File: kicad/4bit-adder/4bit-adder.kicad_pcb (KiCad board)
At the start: 2 copper layers, 4 parts

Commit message: footprints initial layout
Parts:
- added C1: 100uF, Capacitor_THT:CP_Radial_D10.0mm_P2.50mm, F.Cu at (128.5, 214.1)
- added D1: 1N4001, Diode_THT:D_DO-41_SOD81_P10.16mm_Horizontal, F.Cu at (112.1, 51.3)
- added D10: A4 Yellow, LED_THT:LED_D3.0mm, F.Cu at (70.1, 31.3)
- added D11: Carry2 White, LED_THT:LED_D3.0mm, F.Cu at (95.8, 26.8)
- added D12: Carry3 White, LED_THT:LED_D3.0mm, F.Cu at (70.1, 26.8)
- added D13: Sum2 Red, LED_THT:LED_D3.0mm, F.Cu at (96.0, 217.8)
- added D14: Sum3 Red, LED_THT:LED_D3.0mm, F.Cu at (83.1, 217.8)
- added D15: B4 Green, LED_THT:LED_D3.0mm, F.Cu at (70.1, 35.7)
- added D16: A3 Yellow, LED_THT:LED_D3.0mm, F.Cu at (95.8, 31.3)
- added D17: B3 Green, LED_THT:LED_D3.0mm, F.Cu at (95.8, 35.8)
- added D18: A2 Yellow, LED_THT:LED_D3.0mm, F.Cu at (120.6, 31.3)
- added D19: B2 Green, LED_THT:LED_D3.0mm, F.Cu at (120.6, 35.8)
- added D2: A1 Yellow, LED_THT:LED_D3.0mm, F.Cu at (138.9, 31.5)
- added D20: Sum4 Red, LED_THT:LED_D3.0mm, F.Cu at (70.2, 217.7)
- added D21: B1 Green, LED_THT:LED_D3.0mm, F.Cu at (138.9, 36.0)
- added D22: 1N4001, Diode_THT:D_DO-41_SOD81_P10.16mm_Horizontal, F.Cu at (61.1, 52.0)
- added D23: 1N4001, Diode_THT:D_DO-41_SOD81_P10.16mm_Horizontal, F.Cu at (61.1, 67.9)
- added D24: 1N4001, Diode_THT:D_DO-41_SOD81_P10.16mm_Horizontal, F.Cu at (61.1, 73.7)
- added D25: Carry4 Red, LED_THT:LED_D3.0mm, F.Cu at (57.5, 217.5)
- added D26: 1N4001, Diode_THT:D_DO-41_SOD81_P10.16mm_Horizontal, F.Cu at (143.7, 62.4)
- added D27: 1N4001, Diode_THT:D_DO-41_SOD81_P10.16mm_Horizontal, F.Cu at (143.7, 86.7)
- added D28: 1N4001, Diode_THT:D_DO-41_SOD81_P10.16mm_Horizontal, F.Cu at (143.7, 111.2)
- added D29: 1N4001, Diode_THT:D_DO-41_SOD81_P10.16mm_Horizontal, F.Cu at (125.6, 62.4)
- added D3: 1N4001, Diode_THT:D_DO-41_SOD81_P10.16mm_Horizontal, F.Cu at (112.3, 67.5)
- added D30: 1N4001, Diode_THT:D_DO-41_SOD81_P10.16mm_Horizontal, F.Cu at (125.5, 86.5)
- added D31: 1N4001, Diode_THT:D_DO-41_SOD81_P10.16mm_Horizontal, F.Cu at (125.5, 110.8)
- added D32: 1N4001, Diode_THT:D_DO-41_SOD81_P10.16mm_Horizontal, F.Cu at (125.4, 134.8)
- added D33: 1N4001, Diode_THT:D_DO-41_SOD81_P10.16mm_Horizontal, F.Cu at (125.4, 159.1)
- added D34: 1N4001, Diode_THT:D_DO-41_SOD81_P10.16mm_Horizontal, F.Cu at (125.3, 207.6)
- added D35: 1N4001, Diode_THT:D_DO-41_SOD81_P10.16mm_Horizontal, F.Cu at (100.2, 207.4)
- added D36: 1N4001, Diode_THT:D_DO-41_SOD81_P10.16mm_Horizontal, F.Cu at (74.2, 208.3)
- added D37: 1N4001, Diode_THT:D_DO-41_SOD81_P10.16mm_Horizontal, F.Cu at (74.2, 184.0)
- added D38: 1N4001, Diode_THT:D_DO-41_SOD81_P10.16mm_Horizontal, F.Cu at (100.2, 183.2)
- added D39: 1N4001, Diode_THT:D_DO-41_SOD81_P10.16mm_Horizontal, F.Cu at (100.2, 159.1)
- added D4: 1N4001, Diode_THT:D_DO-41_SOD81_P10.16mm_Horizontal, F.Cu at (112.2, 73.3)
- added D40: 1N4001, Diode_THT:D_DO-41_SOD81_P10.16mm_Horizontal, F.Cu at (74.2, 159.8)
- added D41: 1N4001, Diode_THT:D_DO-41_SOD81_P10.16mm_Horizontal, F.Cu at (100.2, 134.9)
- added D42: 1N4001, Diode_THT:D_DO-41_SOD81_P10.16mm_Horizontal, F.Cu at (74.2, 135.5)
- added D43: 1N4001, Diode_THT:D_DO-41_SOD81_P10.16mm_Horizontal, F.Cu at (74.3, 111.3)
- added D44: 1N4001, Diode_THT:D_DO-41_SOD81_P10.16mm_Horizontal, F.Cu at (100.3, 110.7)
- added D45: 1N4001, Diode_THT:D_DO-41_SOD81_P10.16mm_Horizontal, F.Cu at (100.3, 86.5)
- added D46: 1N4001, Diode_THT:D_DO-41_SOD81_P10.16mm_Horizontal, F.Cu at (74.3, 87.1)
- added D47: 1N4001, Diode_THT:D_DO-41_SOD81_P10.16mm_Horizontal, F.Cu at (74.3, 63.0)
- added D48: 1N4001, Diode_THT:D_DO-41_SOD81_P10.16mm_Horizontal, F.Cu at (100.3, 62.1)
- added D49: 1N4001, Diode_THT:D_DO-41_SOD81_P10.16mm_Horizontal, F.Cu at (125.4, 183.3)
- added D5: 1N4001, Diode_THT:D_DO-41_SOD81_P10.16mm_Horizontal, F.Cu at (87.2, 51.1)
- added D6: 1N4001, Diode_THT:D_DO-41_SOD81_P10.16mm_Horizontal, F.Cu at (87.2, 67.5)
- added D7: 1N4001, Diode_THT:D_DO-41_SOD81_P10.16mm_Horizontal, F.Cu at (87.0, 73.2)
- added D8: Sum1 Red, LED_THT:LED_D3.0mm, F.Cu at (108.8, 217.6)
- added D9: Carry1 White, LED_THT:LED_D3.0mm, F.Cu at (120.6, 26.8)
- added J1: Screw_Terminal_01x02, TerminalBlock:TerminalBlock_MaiXu_MX126-5.0-02P_1x02_P5.00mm, F.Cu at (140.4, 212.7)
- added K1: SR11-5V-200-2C-PH, SR11_5V_200_2C:RELAY_SR11-5V-200-2C, F.Cu at (119.2, 50.2)
- added K10: SR11-5V-200-2C-PH, SR11_5V_200_2C:RELAY_SR11-5V-200-2C, F.Cu at (94.0, 50.0)
- added K11: SR11-5V-200-2C-PH, SR11_5V_200_2C:RELAY_SR11-5V-200-2C, F.Cu at (94.0, 74.4)
- added K12: SR11-5V-200-2C-PH, SR11_5V_200_2C:RELAY_SR11-5V-200-2C, F.Cu at (94.0, 98.7)
- added K13: SR11-5V-200-2C-PH, SR11_5V_200_2C:RELAY_SR11-5V-200-2C, F.Cu at (93.9, 122.8)
- added K14: SR11-5V-200-2C-PH, SR11_5V_200_2C:RELAY_SR11-5V-200-2C, F.Cu at (93.9, 147.0)
- added K15: SR11-5V-200-2C-PH, SR11_5V_200_2C:RELAY_SR11-5V-200-2C, F.Cu at (93.9, 171.2)
- added K16: SR11-5V-200-2C-PH, SR11_5V_200_2C:RELAY_SR11-5V-200-2C, F.Cu at (68.0, 50.9)
- added K17: SR11-5V-200-2C-PH, SR11_5V_200_2C:RELAY_SR11-5V-200-2C, F.Cu at (119.0, 195.4)
- added K18: SR11-5V-200-2C-PH, SR11_5V_200_2C:RELAY_SR11-5V-200-2C, F.Cu at (93.8, 195.4)
- added K19: SR11-5V-200-2C-PH, SR11_5V_200_2C:RELAY_SR11-5V-200-2C, F.Cu at (68.0, 75.0)
- added K2: SR11-5V-200-2C-PH, SR11_5V_200_2C:RELAY_SR11-5V-200-2C, F.Cu at (119.3, 74.5)
- added K20: SR11-5V-200-2C-PH, SR11_5V_200_2C:RELAY_SR11-5V-200-2C, F.Cu at (68.0, 99.2)
- added K21: SR11-5V-200-2C-PH, SR11_5V_200_2C:RELAY_SR11-5V-200-2C, F.Cu at (68.0, 123.4)
- added K22: SR11-5V-200-2C-PH, SR11_5V_200_2C:RELAY_SR11-5V-200-2C, F.Cu at (67.9, 147.7)
- added K23: SR11-5V-200-2C-PH, SR11_5V_200_2C:RELAY_SR11-5V-200-2C, F.Cu at (67.9, 171.9)
- added K24: SR11-5V-200-2C-PH, SR11_5V_200_2C:RELAY_SR11-5V-200-2C, F.Cu at (67.9, 196.2)
- added K3: SR11-5V-200-2C-PH, SR11_5V_200_2C:RELAY_SR11-5V-200-2C, F.Cu at (119.1, 98.5)
- added K4: SR11-5V-200-2C-PH, SR11_5V_200_2C:RELAY_SR11-5V-200-2C, F.Cu at (119.1, 122.8)
- added K5: SR11-5V-200-2C-PH, SR11_5V_200_2C:RELAY_SR11-5V-200-2C, F.Cu at (119.1, 147.0)
- added K6: SR11-5V-200-2C-PH, SR11_5V_200_2C:RELAY_SR11-5V-200-2C, F.Cu at (119.1, 171.1)
- added K7: SR11-5V-200-2C-PH, SR11_5V_200_2C:RELAY_SR11-5V-200-2C, F.Cu at (137.4, 50.3)
- added K8: SR11-5V-200-2C-PH, SR11_5V_200_2C:RELAY_SR11-5V-200-2C, F.Cu at (137.4, 74.5)
- added K9: SR11-5V-200-2C-PH, SR11_5V_200_2C:RELAY_SR11-5V-200-2C, F.Cu at (137.4, 99.0)
- added R10: 470, Resistor_THT:R_Axial_DIN0207_L6.3mm_D2.5mm_P10.16mm_Horizontal, F.Cu at (57.7, 31.2)
- added R11: 470, Resistor_THT:R_Axial_DIN0207_L6.3mm_D2.5mm_P10.16mm_Horizontal, F.Cu at (83.0, 214.8)
- added R12: 470, Resistor_THT:R_Axial_DIN0207_L6.3mm_D2.5mm_P10.16mm_Horizontal, F.Cu at (70.3, 214.8)
- added R13: 470, Resistor_THT:R_Axial_DIN0207_L6.3mm_D2.5mm_P10.16mm_Horizontal, F.Cu at (57.6, 214.8)
- added R15: 470, Resistor_THT:R_Axial_DIN0207_L6.3mm_D2.5mm_P10.16mm_Horizontal, F.Cu at (57.7, 35.9)
- added R16: 470, Resistor_THT:R_Axial_DIN0207_L6.3mm_D2.5mm_P10.16mm_Horizontal, F.Cu at (83.5, 31.3)
- added R17: 470, Resistor_THT:R_Axial_DIN0207_L6.3mm_D2.5mm_P10.16mm_Horizontal, F.Cu at (83.5, 35.7)
- added R18: 470, Resistor_THT:R_Axial_DIN0207_L6.3mm_D2.5mm_P10.16mm_Horizontal, F.Cu at (108.1, 31.3)
- added R19: 470, Resistor_THT:R_Axial_DIN0207_L6.3mm_D2.5mm_P10.16mm_Horizontal, F.Cu at (108.2, 35.8)
- added R2: 470, Resistor_THT:R_Axial_DIN0207_L6.3mm_D2.5mm_P10.16mm_Horizontal, F.Cu at (126.5, 31.5)
- added R20: 470, Resistor_THT:R_Axial_DIN0207_L6.3mm_D2.5mm_P10.16mm_Horizontal, F.Cu at (108.2, 26.8)
- added R21: 470, Resistor_THT:R_Axial_DIN0207_L6.3mm_D2.5mm_P10.16mm_Horizontal, F.Cu at (126.5, 36.0)
- added R22: 470, Resistor_THT:R_Axial_DIN0207_L6.3mm_D2.5mm_P10.16mm_Horizontal, F.Cu at (83.5, 26.9)
- added R23: 470, Resistor_THT:R_Axial_DIN0207_L6.3mm_D2.5mm_P10.16mm_Horizontal, F.Cu at (57.8, 26.8)
- added R8: 470, Resistor_THT:R_Axial_DIN0207_L6.3mm_D2.5mm_P10.16mm_Horizontal, F.Cu at (108.8, 214.8)
- added R9: 470, Resistor_THT:R_Axial_DIN0207_L6.3mm_D2.5mm_P10.16mm_Horizontal, F.Cu at (96.0, 214.8)
- added SW1: SW_Wuerth_450301014042, Button_Switch_THT:SW_Slide-03_Wuerth-WS-SLTV_10x2.5x6.4_P2.54mm, F.Cu at (139.7, 204.8)
- added SW3: A, Button_Switch_THT:SW_DIP_SPSTx04_Piano_10.8x11.72mm_W7.62mm_P2.54mm, F.Cu at (134.5, 172.6)
- added SW4: B, Button_Switch_THT:SW_DIP_SPSTx04_Piano_10.8x11.72mm_W7.62mm_P2.54mm, F.Cu at (134.5, 189.6)

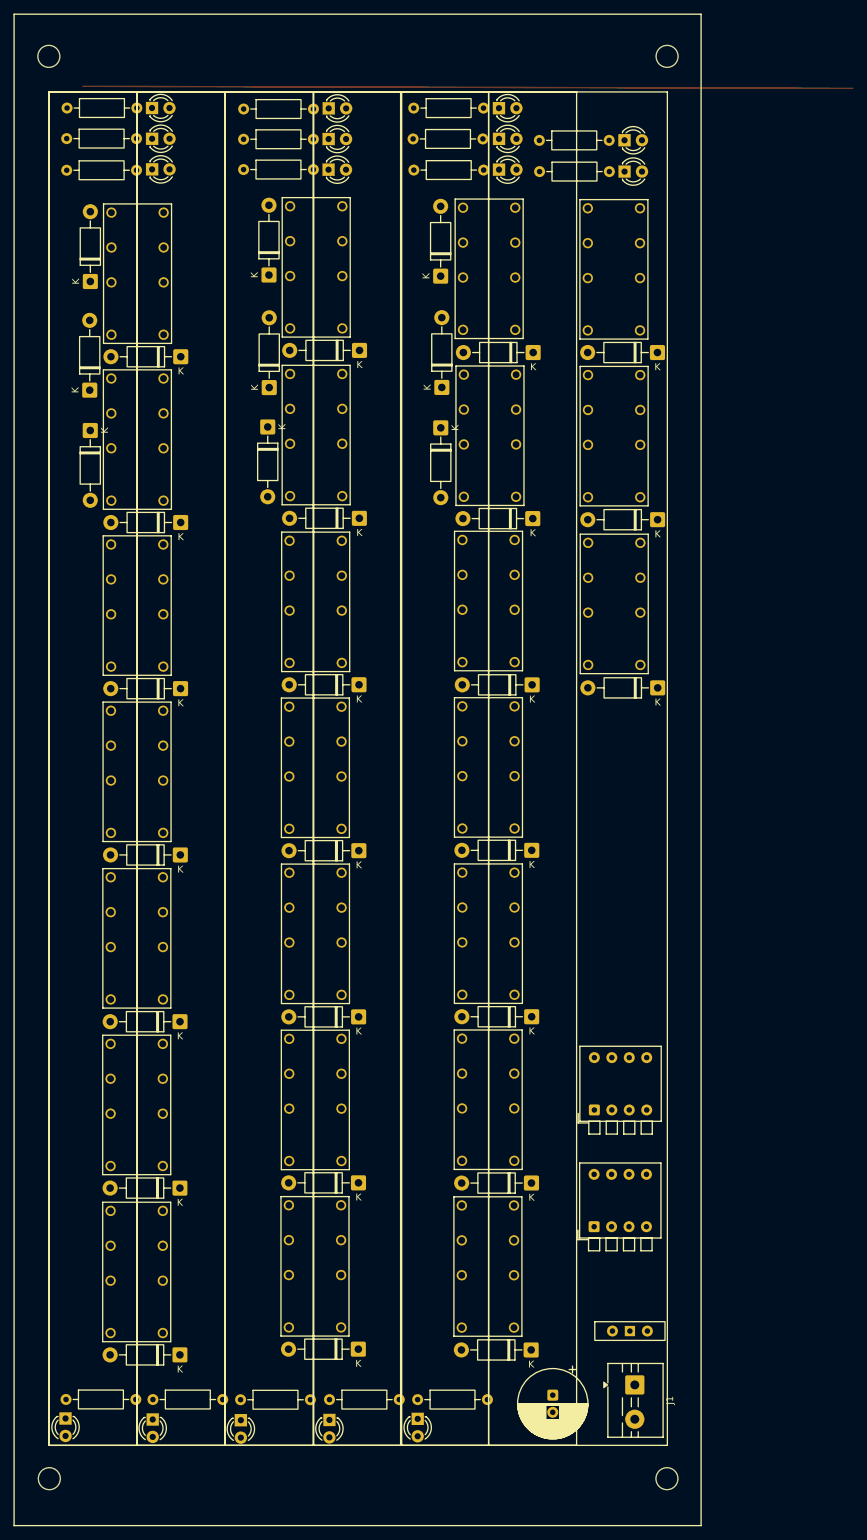
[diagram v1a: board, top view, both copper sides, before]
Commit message: wired top pad-A
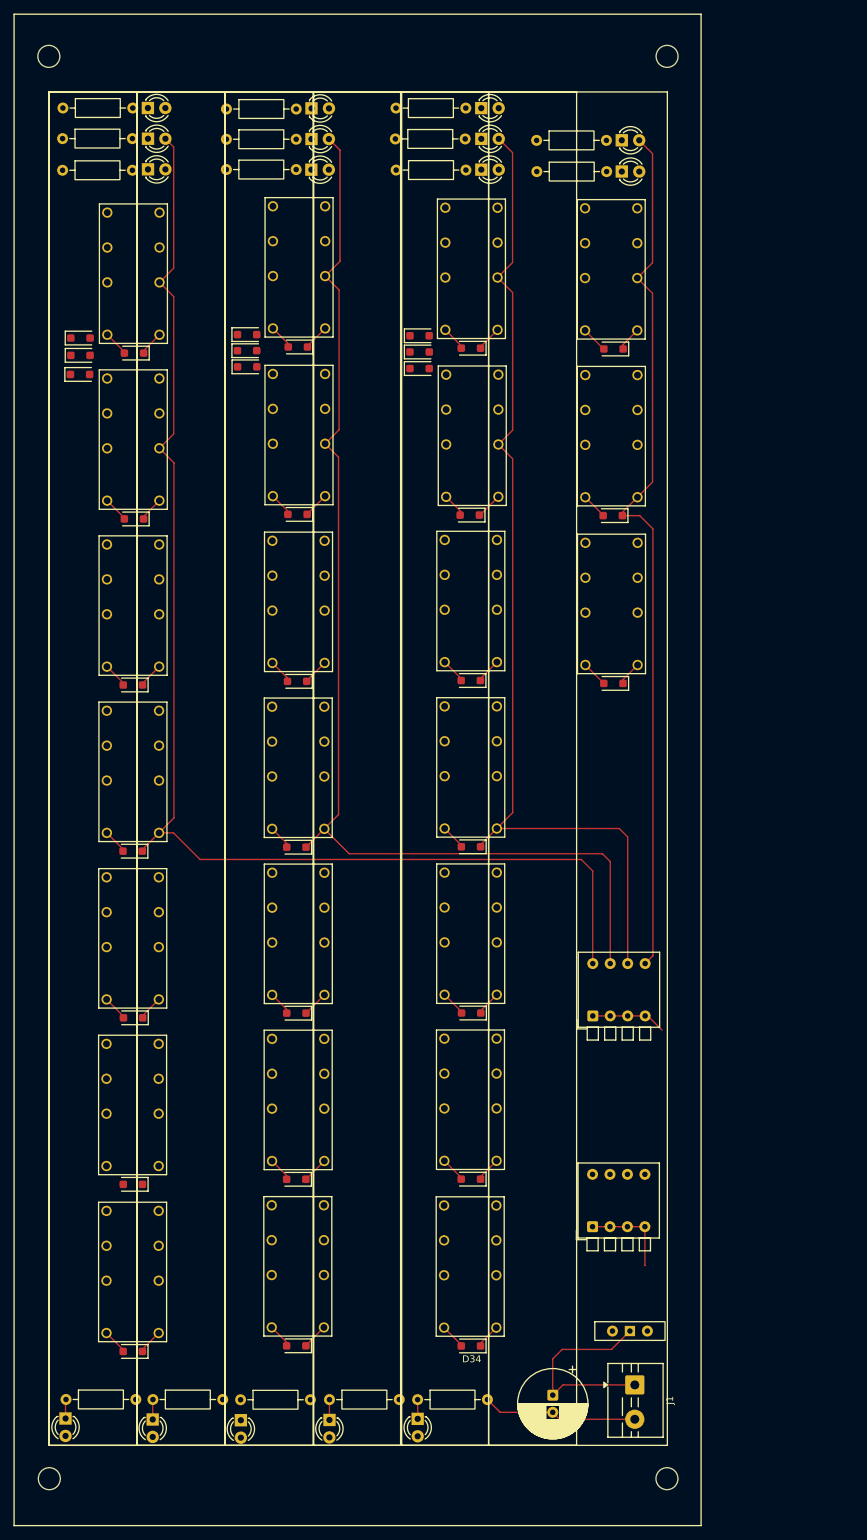
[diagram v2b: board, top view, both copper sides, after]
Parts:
- D1, D22, D23, D24, D26, D27, D28, D29, D3, D30, D31, D32, D33, D34, D35, D36, D37, D38, D39, D4, D40, D41, D42, D43, D44, D45, D46, D47, D48, D49, D5, D6, D7: footprint Diode_THT:D_DO-41_SOD81_P10.16mm_Horizontal -> Diode_SMD:D_SOD-123F
- moved SW3 13.7 mm to (134.3, 158.9)
- moved D7 9.24 mm to (84.0, 64.5), turned to 0 degrees
- moved D5 9.23 mm to (84.0, 59.8), turned to 0 degrees
- moved D1 9.21 mm to (109.1, 59.9), turned to 0 degrees
- moved D30 9.19 mm to (116.4, 86.0)
- moved D4 9.17 mm to (109.1, 64.7), turned to 0 degrees
- moved D41 9.10 mm to (91.1, 134.4)
- moved D29 9.09 mm to (116.5, 61.8)
- moved D39 9.08 mm to (91.1, 158.5)
- moved D38 9.07 mm to (91.1, 182.7)
- moved D35 9.04 mm to (91.1, 207.0)
- moved D44 9.02 mm to (91.2, 110.2)
- moved D45 9.02 mm to (91.3, 85.9)
- moved D48 8.99 mm to (91.4, 61.6)
- moved D31 8.95 mm to (116.5, 110.1)
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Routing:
- net Net-(D10-A): track 0.00 -> 188.5 mm
- net Net-(D16-A): track 0.00 -> 167.5 mm
- net Net-(D18-A): track 0.00 -> 147.3 mm
- net Net-(D2-A): track 0.00 -> 128.1 mm
- net GND: track 0.00 -> 106.6 mm
- net Net-(J1-Pin_1): track 0.00 -> 30.7 mm
- net SWV: track 0.00 -> 24.2 mm
- net Net-(D1-K): track 0.00 -> 11.3 mm
- net Net-(D30-K): track 0.00 -> 11.2 mm
- net Net-(D12-A): track 0.00 -> 11.0 mm
- net Net-(D17-A): track 0.00 -> 7.55 mm
- net Net-(D19-A): track 0.00 -> 7.32 mm
- net Net-(D15-A): track 0.00 -> 7.28 mm
- net Net-(D21-A): track 0.00 -> 7.11 mm
- net Net-(D38-K): track 0.00 -> 3.78 mm
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
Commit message: finished pcb wiring
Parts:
- D1, D22, D23, D24, D26, D27, D28, D29, D3, D30, D31, D32, D33, D34, D35, D36, D37, D38, D39, D4, D40, D41, D42, D43, D44, D45, D46, D47, D48, D49, D5, D6, D7: footprint Diode_SMD:D_SOD-123F -> Diode_THT:D_T-1_P5.08mm_Horizontal
- moved R10 11.0 mm to (68.1, 31.5), turned to 180 degrees
- moved R16 11.0 mm to (91.9, 31.6), turned to 180 degrees
- moved R18 11.0 mm to (116.5, 31.5), turned to 180 degrees
- moved R20 10.9 mm to (116.6, 27.1), turned to 180 degrees
- moved R15 10.9 mm to (68.0, 36.0), turned to 180 degrees
- moved R19 10.9 mm to (116.5, 36.0), turned to 180 degrees
- moved R21 10.9 mm to (137.0, 36.2), turned to 180 degrees
- moved R23 10.9 mm to (68.0, 27.1), turned to 180 degrees
- moved R17 10.8 mm to (91.8, 36.1), turned to 180 degrees
- moved R22 10.8 mm to (91.8, 27.1), turned to 180 degrees
- moved D35 4.01 mm to (95.1, 207.6)
- moved D38 3.98 mm to (95.0, 183.4)
- moved D48 3.87 mm to (95.2, 62.2)
- moved D39 3.87 mm to (94.9, 159.3)
- moved D44 3.87 mm to (95.1, 110.9)
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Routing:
- net GND: track 106.6 -> 888.4 mm, vias 0 -> 6
- net SWV: track 24.2 -> 379.4 mm
- net Net-(D12-A): track 11.0 -> 229.7 mm, vias 0 -> 3
- net Net-(D30-K): track 11.2 -> 216.7 mm, vias 0 -> 5
- net Net-(D15-A): track 7.28 -> 210.7 mm, vias 0 -> 2
- net Net-(D1-K): track 11.3 -> 208.4 mm, vias 0 -> 3
- net Net-(D17-A): track 7.55 -> 190.4 mm, vias 0 -> 2
- net Net-(D19-A): track 7.32 -> 169.2 mm, vias 0 -> 4
- net Net-(D8-A): track 0.00 -> 161.9 mm, vias 0 -> 1
- net Net-(D22-K): track 0.00 -> 161.1 mm
- net Net-(D21-A): track 7.11 -> 160.1 mm, vias 0 -> 2
- net Net-(D49-K): track 3.64 -> 49.6 mm, vias 0 -> 4
- net Net-(D37-K): track 0.00 -> 42.5 mm
- net Net-(D38-K): track 3.78 -> 45.1 mm, vias 0 -> 3
- net Net-(K4-PadNO2): track 0.00 -> 37.0 mm, vias 0 -> 2
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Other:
- board outline added: 100.1 x 220.1 mm
